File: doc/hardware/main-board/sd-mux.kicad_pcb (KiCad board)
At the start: 2 copper layers, 50 x 114 mm, 52 parts, among them J1 USDCARD, P1 USB_OTG, P10 PINS 1,5x3, P2 629105136821, P3 61400416021, P4 61400416021, P5 IDC_02X04, P6 IDC_02X04, P7 PINS 1,5x3, P8 CONN_02X02, P9 CONN_02X02, Q1 IRF7606PBF, Q2 IRF7606PBF, Q3 IRF7606PBF, Q4 IRF7606PBF, Q5 2N7002, Q6 2N7002, Q7 IRF7606PBF, Q8 IRF7606PBF, U1 TS3USB30EDGSR, U2 FT245RL, U3 74AHC1G14, U4 TS3A27518E, U5 74AHC1G14

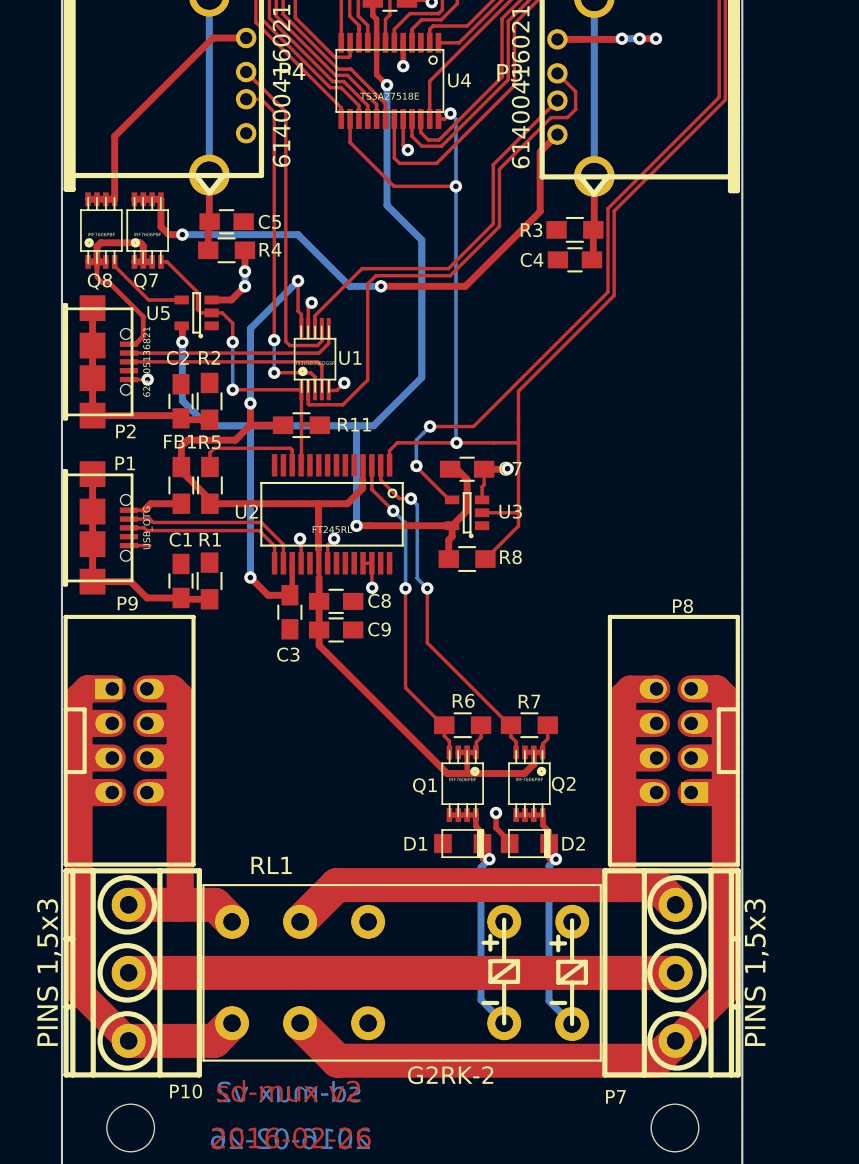
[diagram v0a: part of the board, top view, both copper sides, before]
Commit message: Fix power supply connection of USB switch inverter
Power supply pin of U5 was connected to 3.3V. Q8, driven from this
inverter, couldn't be fully closed as maximum output voltage from
the inverter was 3.3V. Now, the inverter, is connected to VCC pin
of USB connector which gives 5V.

Change-Id: Ibed75765ea8cbc2727066d6a498a3396a2d3c404
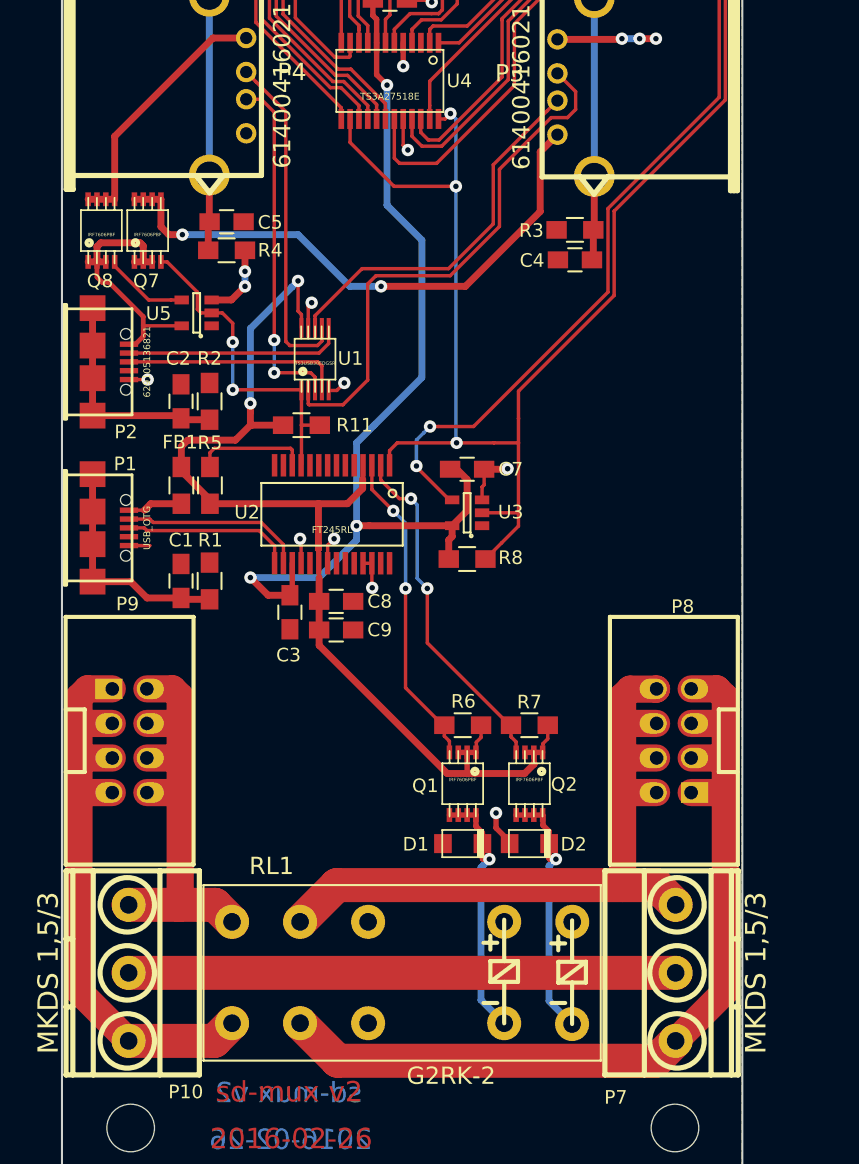
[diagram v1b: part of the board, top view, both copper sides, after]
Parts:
- P10, P7: value PINS 1,5x3 -> MKDS 1,5/3
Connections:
- U5 pad 5: +3V3 -> Net-(P2-Pad1)
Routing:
- net +3V3: track 94.0 -> 73.1 mm, vias 4 -> 3
- net Net-(P2-Pad1): track 17.0 -> 19.9 mm
